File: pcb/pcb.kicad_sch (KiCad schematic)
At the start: 18 parts

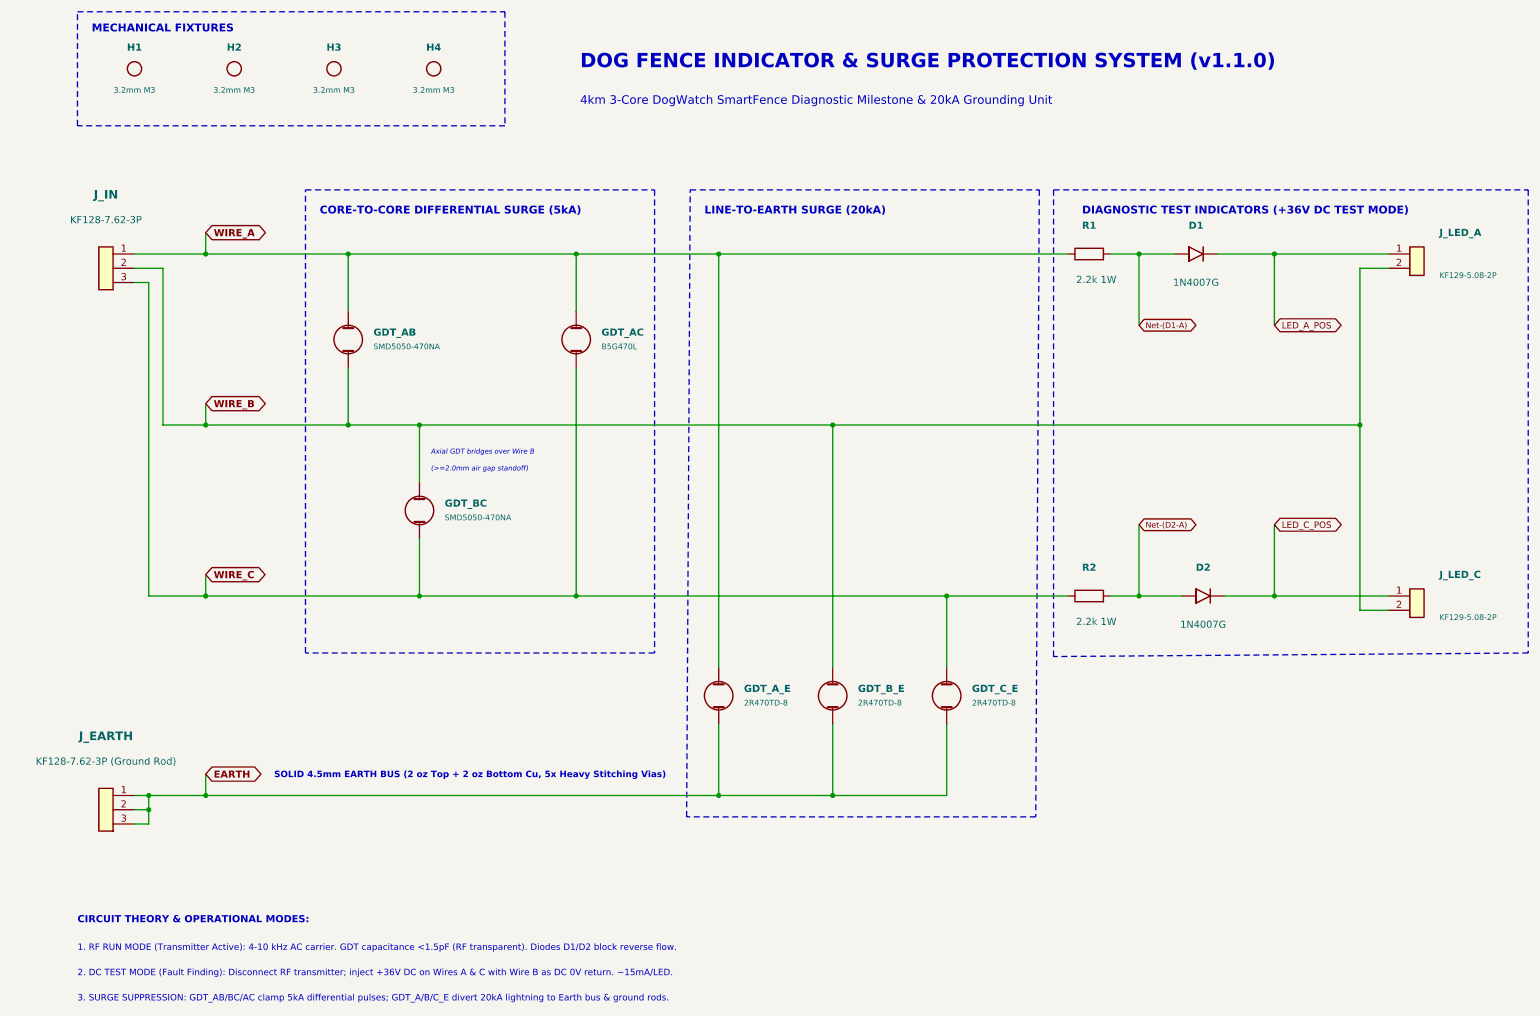
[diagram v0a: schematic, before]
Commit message: Implement guarded remediation and manufacturing verification
Add complete-project checks, native manufacturing validation, electrical regressions, and bounded PCB/library corrections for 1.2.0-dev. Preserve unresolved protection, fit/process, and hardware qualification holds.
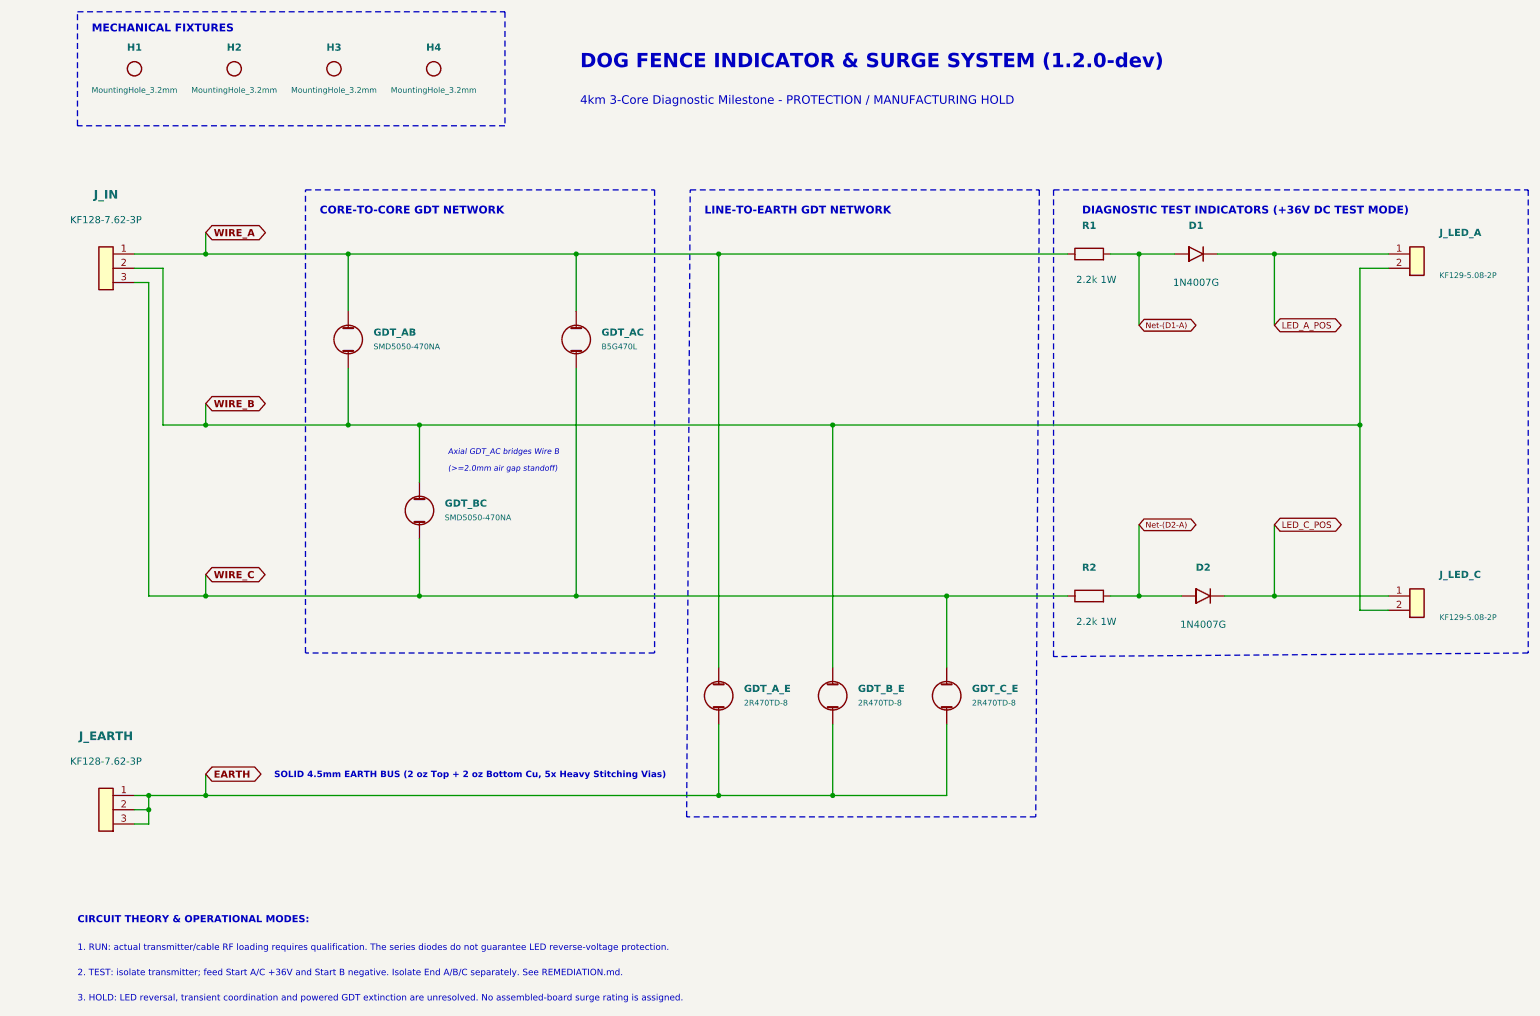
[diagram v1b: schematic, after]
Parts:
- D1, D2: footprint Diode_THT:D_DO-41_SOD81_P10.16mm_Horizontal -> DogFence:1N4007G_P10.16mm_K_Right; symbol Device:D -> DogFence:D_A_Left_K_Right; Manufacturer (none) -> onsemi
- GDT_AB, GDT_BC: footprint GDT_SMD:GDT_SMD_5.0x5.0mm -> DogFence:SMD5050-470NA; symbol Device:GDT -> DogFence:GDT; Manufacturer (none) -> Ruilon
- GDT_AC: footprint Resistor_THT:R_Axial_DIN0617_L17.0mm_D6.0mm_P15.24mm_Horizontal -> DogFence:B5G470L_P15.24mm_NS_Overpass; symbol Device:GDT -> DogFence:GDT; Manufacturer (none) -> Bencent
- GDT_A_E, GDT_B_E, GDT_C_E: footprint Resistor_THT:R_Axial_DIN0617_L17.0mm_D6.0mm_P15.24mm_Horizontal -> DogFence:2R470TD-8_P15.24mm; symbol Device:GDT -> DogFence:GDT; Manufacturer (none) -> Ruilon
- H1, H2, H3, H4: value 3.2mm M3 -> MountingHole_3.2mm; footprint MountingHole:MountingHole_3.2mm_M3 -> DogFence:MountingHole_3.2mm; symbol Mechanical:MountingHole -> DogFence:MountingHole; now left out of the parts list
- J_EARTH: value KF128-7.62-3P (Ground Rod) -> KF128-7.62-3P; footprint TerminalBlock_Phoenix:TerminalBlock_Phoenix_MKDS-1,5-3-7.62_1x03_P7.62mm_Horizontal -> DogFence:KF128_7.62_3P_Earth; symbol Connector_Generic:Conn_01x03 -> DogFence:Conn_01x03; Manufacturer (none) -> Cixi Kefa Elec
- J_IN: footprint TerminalBlock_Phoenix:TerminalBlock_Phoenix_MKDS-1,5-3-7.62_1x03_P7.62mm_Horizontal -> DogFence:KF128_7.62_3P_Input; symbol Connector_Generic:Conn_01x03 -> DogFence:Conn_01x03; Manufacturer (none) -> Cixi Kefa Elec
- J_LED_A: footprint TerminalBlock_Phoenix:TerminalBlock_Phoenix_MKDS-1,5-2-5.08_1x02_P5.08mm_Horizontal -> DogFence:KF129_5.08_2P_LED_A; symbol Connector_Generic:Conn_01x02 -> DogFence:Conn_01x02; Manufacturer (none) -> Cixi Kefa Elec
- J_LED_C: footprint TerminalBlock_Phoenix:TerminalBlock_Phoenix_MKDS-1,5-2-5.08_1x02_P5.08mm_Horizontal -> DogFence:KF129_5.08_2P_LED_C; symbol Connector_Generic:Conn_01x02 -> DogFence:Conn_01x02; Manufacturer (none) -> Cixi Kefa Elec
- R1, R2: footprint Resistor_THT:R_Axial_DIN0414_L11.9mm_D4.5mm_P15.24mm_Horizontal -> DogFence:MBE0414_P15.24mm; symbol Device:R -> DogFence:R; Manufacturer (none) -> Vishay Intertech
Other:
- note added: "1. RUN: actual transmitter/cable RF loading requires qualification. The series diodes do not guarantee LED reverse-voltage protection."
- note added: "2. TEST: isolate transmitter; feed Start A/C +36V and Start B negative. Isolate End A/B/C separately. See REMEDIATION.md."
- note added: "3. HOLD: LED reversal, transient coordination and powered GDT extinction are unresolved. No assembled-board surge rating is assigned."
- note added: "4km 3-Core Diagnostic Milestone - PROTECTION / MANUFACTURING HOLD"
- note added: "Axial GDT_AC bridges Wire B"
- note added: "CORE-TO-CORE GDT NETWORK"
- note added: "DOG FENCE INDICATOR & SURGE SYSTEM (1.2.0-dev)"
- note added: "LINE-TO-EARTH GDT NETWORK"
- note removed: "1. RF RUN MODE (Transmitter Active): 4-10 kHz AC carrier. GDT capacitance <1.5pF (RF transparent). Diodes D1/D2 block reverse flow."
- note removed: "2. DC TEST MODE (Fault Finding): Disconnect RF transmitter; inject +36V DC on Wires A & C with Wire B as DC 0V return. ~15mA/LED."
- note removed: "3. SURGE SUPPRESSION: GDT_AB/BC/AC clamp 5kA differential pulses; GDT_A/B/C_E divert 20kA lightning to Earth bus & ground rods."
- note removed: "4km 3-Core DogWatch SmartFence Diagnostic Milestone & 20kA Grounding Unit"
- note removed: "Axial GDT bridges over Wire B"
- note removed: "CORE-TO-CORE DIFFERENTIAL SURGE (5kA)"
- note removed: "DOG FENCE INDICATOR & SURGE PROTECTION SYSTEM (v1.1.0)"
- note removed: "LINE-TO-EARTH SURGE (20kA)"

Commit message: Add diode to PCB to prevent reverse flow across LEDs
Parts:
- added D3, D4: BYG23T-M3, DogFence:BYG23T_SMA_K_Right, symbol DogFence:D_A_Left_K_Right
- D1, D2: value 1N4007G -> BYG23T-M3; footprint DogFence:1N4007G_P10.16mm_K_Right -> DogFence:BYG23T_SMA_K_Right; LCSC C232439 -> C145454; MPN 1N4007G -> BYG23T-M3/TR; Manufacturer onsemi -> Vishay General Semiconductor; Sourcing (none) -> LCSC
- GDT_AB, GDT_AC, GDT_A_E, GDT_BC, GDT_B_E, GDT_C_E, J_EARTH, J_IN, J_LED_A, J_LED_C: Sourcing (none) -> LCSC
- R1, R2: value 2.2k 1W -> 2.2k 2W; footprint DogFence:MBE0414_P15.24mm -> DogFence:PR02_Cu_P15.24mm; LCSC C1368610 -> (none); MPN MBE04140C2201FC100 -> PR02000202201FA100; Manufacturer Vishay Intertech -> Vishay BCcomponents; Sourcing (none) -> External; Sourcing Reference (none) -> https://www.vishay.com/search?type=inv&query=PR02000202201F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
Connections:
- net LED_A_POS: now also D3.1 (K)
- net LED_C_POS: now also D4.1 (K)
- net WIRE_B: now also D3.2 (A), D4.2 (A)
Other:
- note added: "1. RUN: RF/transient qualification held. D3/D4 clamp negative LED outputs; no reversed flying-lead immunity."
- note added: "2. TEST: isolate transmitter; Start A/C +36V, Start B negative; End A/B/C separately isolated. Continuous-safe duty required; containment disabled."
- note added: "3. HOLD: thermal and powered-GDT recovery unqualified; no board surge rating. Energized cattle fencing prohibited along the entire boundary."
- note removed: "1. RUN: actual transmitter/cable RF loading requires qualification. The series diodes do not guarantee LED reverse-voltage protection."
- note removed: "2. TEST: isolate transmitter; feed Start A/C +36V and Start B negative. Isolate End A/B/C separately. See REMEDIATION.md."
- note removed: "3. HOLD: LED reversal, transient coordination and powered GDT extinction are unresolved. No assembled-board surge rating is assigned."

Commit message: Split prototype/gerbers and release/production makefile output and gates
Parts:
- R1, R2: footprint DogFence:PR02_Cu_P15.24mm -> DogFence:R_2512_6332Metric; LCSC (none) -> C2791283; MPN PR02000202201FA100 -> HP122WF2201T4E; Manufacturer Vishay BCcomponents -> Uni-Royal; Sourcing External -> LCSC; Sourcing Reference https://www.vishay.com/search?type=inv&query=PR02000202201F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 -> (none)
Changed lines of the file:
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@@
 			)
 		)
-		(property "Manufacturer" "Vishay BCcomponents"
+		(property "Manufacturer" "Uni-Royal"
 			(at 205.74 62.23 0)
 			(effects
@@
 			)
 		)
-		(property "Footprint" "DogFence:PR02_Cu_P15.24mm"
+		(property "Footprint" "DogFence:R_2512_6332Metric"
 			(at 205.74 62.23 90)
 			(effects
@@
 			)
 		)
-		(property "Datasheet" "https://www.vishay.com/docs/28729/pr010203.pdf"
+		(property "Datasheet" "https://www.lcsc.com"
 			(at 205.74 62.23 0)
 			(effects
@@
 			)
 		)
-		(property "Description" "Vishay PR02000202201FA100; 2.2k 2W 1%, +/-250ppm/K; Cu lead 0.78 +/-0.05mm, body L2 <=12.0mm D <=3.9mm; require >=1.00mm body-to-PCB standoff; forming/process and continuous TEST thermal qualification held"
+		(property "Description" "Uni-Royal HP122WF2201T4E; 2.2k 2W 1% 2512 SMD chip resistor"
 			(at 205.74 62.23 0)
 			(effects
@@
 			)
 		)
-		(property "MPN" "PR02000202201FA100"
+		(property "MPN" "HP122WF2201T4E"
 			(at 205.74 62.23 0)
 			(effects
@@
 			)
 		)
-		(property "LCSC" ""
+		(property "LCSC" "C2791283"
 			(at 205.74 62.23 0)
 			(effects
@@
 			)
 		)
-		(property "Sourcing" "External"
+		(property "Sourcing" "LCSC"
 			(at 205.74 62.23 0)
 			(effects
@@
 			)
 		)
-		(property "Sourcing Reference" "https://www.vishay.com/search?type=inv&query=PR02000202201FA100"
+		(property "Sourcing Reference" ""
 			(at 205.74 62.23 0)
 			(effects
@@
 			)
 		)
-		(property "Manufacturer" "Vishay BCcomponents"
+		(property "Manufacturer" "Uni-Royal"
 			(at 205.74 123.19 0)
 			(effects
@@
 			)
 		)
-		(property "Footprint" "DogFence:PR02_Cu_P15.24mm"
+		(property "Footprint" "DogFence:R_2512_6332Metric"
 			(at 205.74 123.19 90)
 			(effects
@@
 			)
 		)
-		(property "Datasheet" "https://www.vishay.com/docs/28729/pr010203.pdf"
+		(property "Datasheet" "https://www.lcsc.com"
 			(at 205.74 123.19 0)
 			(effects
@@
 			)
 		)
-		(property "Description" "Vishay PR02000202201FA100; 2.2k 2W 1%, +/-250ppm/K; Cu lead 0.78 +/-0.05mm, body L2 <=12.0mm D <=3.9mm; require >=1.00mm body-to-PCB standoff; forming/process and continuous TEST thermal qualification held"
+		(property "Description" "Uni-Royal HP122WF2201T4E; 2.2k 2W 1% 2512 SMD chip resistor"
 			(at 205.74 123.19 0)
 			(effects
@@
 			)
 		)
-		(property "MPN" "PR02000202201FA100"
+		(property "MPN" "HP122WF2201T4E"
 			(at 205.74 123.19 0)
 			(effects
@@
 			)
 		)
-		(property "LCSC" ""
+		(property "LCSC" "C2791283"
 			(at 205.74 123.19 0)
 			(effects
@@
 			)
 		)
-		(property "Sourcing" "External"
+		(property "Sourcing" "LCSC"
 			(at 205.74 123.19 0)
 			(effects
@@
 			)
 		)
-		(property "Sourcing Reference" "https://www.vishay.com/search?type=inv&query=PR02000202201FA100"
+		(property "Sourcing Reference" ""
 			(at 205.74 123.19 0)
 			(effects

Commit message: Review of Gemini simplification by GPT
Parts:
- R1, R2: LCSC C2791283 -> (none); Sourcing LCSC -> External; Sourcing Reference (none) -> https://store.nacsemi.com/products/detail?stock=XSJMZ000001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
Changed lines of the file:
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@@
 			)
 		)
-		(property "Datasheet" "https://www.lcsc.com"
+		(property "Datasheet" "https://www.uni-royal.cn/en/images/userfile/file/1784806233a2e6d381ea80b5d9.pdf"
 			(at 205.74 62.23 0)
 			(effects
@@
 			)
 		)
-		(property "LCSC" "C2791283"
+		(property "LCSC" ""
 			(at 205.74 62.23 0)
 			(effects
@@
 			)
 		)
-		(property "Sourcing" "LCSC"
+		(property "Sourcing" "External"
 			(at 205.74 62.23 0)
 			(effects
@@
 			)
 		)
-		(property "Sourcing Reference" ""
+		(property "Sourcing Reference" "https://store.nacsemi.com/products/detail?stock=XSJMZ0000010410"
 			(at 205.74 62.23 0)
 			(effects
@@
 			)
 		)
-		(property "Datasheet" "https://www.lcsc.com"
+		(property "Datasheet" "https://www.uni-royal.cn/en/images/userfile/file/1784806233a2e6d381ea80b5d9.pdf"
 			(at 205.74 123.19 0)
 			(effects
@@
 			)
 		)
-		(property "LCSC" "C2791283"
+		(property "LCSC" ""
 			(at 205.74 123.19 0)
 			(effects
@@
 			)
 		)
-		(property "Sourcing" "LCSC"
+		(property "Sourcing" "External"
 			(at 205.74 123.19 0)
 			(effects
@@
 			)
 		)
-		(property "Sourcing Reference" ""
+		(property "Sourcing Reference" "https://store.nacsemi.com/products/detail?stock=XSJMZ0000010410"
 			(at 205.74 123.19 0)
 			(effects

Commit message: Finalize R1/R2 as Uni-Royal PS122WF2201T4E
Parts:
- R1, R2: LCSC (none) -> C2793873; MPN HP122WF2201T4E -> PS122WF2201T4E; Sourcing External -> LCSC; Sourcing Reference https://store.nacsemi.com/products/detail?stock=XSJMZ000001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 -> (none)
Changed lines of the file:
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@@
 			)
 		)
-		(property "Datasheet" "https://www.uni-royal.cn/en/images/userfile/file/1784806233a2e6d381ea80b5d9.pdf"
+		(property "Datasheet" "https://www.uni-royal.cn/en/images/userfile/file/1784854235b7c79f8d8a205c5d.pdf"
 			(at 205.74 62.23 0)
 			(effects
@@
 			)
 		)
-		(property "Description" "Uni-Royal HP122WF2201T4E; 2.2k 2W 1% 2512 SMD chip resistor"
+		(property "Description" "Uni-Royal PS122WF2201T4E C2793873; 2.2k 2W 1% PS12/2512 SMD chip resistor; prototype and production"
 			(at 205.74 62.23 0)
 			(effects
@@
 			)
 		)
-		(property "MPN" "HP122WF2201T4E"
+		(property "MPN" "PS122WF2201T4E"
 			(at 205.74 62.23 0)
 			(effects
@@
 			)
 		)
-		(property "LCSC" ""
+		(property "LCSC" "C2793873"
 			(at 205.74 62.23 0)
 			(effects
@@
 			)
 		)
-		(property "Sourcing" "External"
+		(property "Sourcing" "LCSC"
 			(at 205.74 62.23 0)
 			(effects
@@
 			)
 		)
-		(property "Sourcing Reference" "https://store.nacsemi.com/products/detail?stock=XSJMZ0000010410"
+		(property "Sourcing Reference" ""
 			(at 205.74 62.23 0)
 			(effects
@@
 			)
 		)
-		(property "Datasheet" "https://www.uni-royal.cn/en/images/userfile/file/1784806233a2e6d381ea80b5d9.pdf"
+		(property "Datasheet" "https://www.uni-royal.cn/en/images/userfile/file/1784854235b7c79f8d8a205c5d.pdf"
 			(at 205.74 123.19 0)
 			(effects
@@
 			)
 		)
-		(property "Description" "Uni-Royal HP122WF2201T4E; 2.2k 2W 1% 2512 SMD chip resistor"
+		(property "Description" "Uni-Royal PS122WF2201T4E C2793873; 2.2k 2W 1% PS12/2512 SMD chip resistor; prototype and production"
 			(at 205.74 123.19 0)
 			(effects
@@
 			)
 		)
-		(property "MPN" "HP122WF2201T4E"
+		(property "MPN" "PS122WF2201T4E"
 			(at 205.74 123.19 0)
 			(effects
@@
 			)
 		)
-		(property "LCSC" ""
+		(property "LCSC" "C2793873"
 			(at 205.74 123.19 0)
 			(effects
@@
 			)
 		)
-		(property "Sourcing" "External"
+		(property "Sourcing" "LCSC"
 			(at 205.74 123.19 0)
 			(effects
@@
 			)
 		)
-		(property "Sourcing Reference" "https://store.nacsemi.com/products/detail?stock=XSJMZ0000010410"
+		(property "Sourcing Reference" ""
 			(at 205.74 123.19 0)
 			(effects

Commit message: Move to a TE R1/R2 prototype with Yageo for production
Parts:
- R1, R2: LCSC C2793873 -> C4129105; MPN PS122WF2201T4E -> 35212K2FT; Manufacturer Uni-Royal -> TE Connectivity
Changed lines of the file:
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@@
 			)
 		)
-		(property "Manufacturer" "Uni-Royal"
+		(property "Manufacturer" "TE Connectivity"
 			(at 205.74 62.23 0)
 			(effects
@@
 			)
 		)
-		(property "Datasheet" "https://www.uni-royal.cn/en/images/userfile/file/1784854235b7c79f8d8a205c5d.pdf"
+		(property "Datasheet" "https://www.te.com/commerce/DocumentDelivery/DDEController?Action=showdoc&DocId=Data+Sheet%7F9-1773463-5%7FG1%7Fpdf%7FEnglish%7FENG_DS_9-1773463-5_G1.pdf"
 			(at 205.74 62.23 0)
 			(effects
@@
 			)
 		)
-		(property "Description" "Uni-Royal PS122WF2201T4E C2793873; 2.2k 2W 1% PS12/2512 SMD chip resistor; prototype and production"
+		(property "Description" "TE Connectivity 35212K2FT C4129105; 2.2k 2W 1% 3521/2512 SMD chip resistor; prototype selection"
 			(at 205.74 62.23 0)
 			(effects
@@
 			)
 		)
-		(property "MPN" "PS122WF2201T4E"
+		(property "MPN" "35212K2FT"
 			(at 205.74 62.23 0)
 			(effects
@@
 			)
 		)
-		(property "LCSC" "C2793873"
+		(property "LCSC" "C4129105"
 			(at 205.74 62.23 0)
 			(effects
@@
 			)
 		)
-		(property "Manufacturer" "Uni-Royal"
+		(property "Manufacturer" "TE Connectivity"
 			(at 205.74 123.19 0)
 			(effects
@@
 			)
 		)
-		(property "Datasheet" "https://www.uni-royal.cn/en/images/userfile/file/1784854235b7c79f8d8a205c5d.pdf"
+		(property "Datasheet" "https://www.te.com/commerce/DocumentDelivery/DDEController?Action=showdoc&DocId=Data+Sheet%7F9-1773463-5%7FG1%7Fpdf%7FEnglish%7FENG_DS_9-1773463-5_G1.pdf"
 			(at 205.74 123.19 0)
 			(effects
@@
 			)
 		)
-		(property "Description" "Uni-Royal PS122WF2201T4E C2793873; 2.2k 2W 1% PS12/2512 SMD chip resistor; prototype and production"
+		(property "Description" "TE Connectivity 35212K2FT C4129105; 2.2k 2W 1% 3521/2512 SMD chip resistor; prototype selection"
 			(at 205.74 123.19 0)
 			(effects
@@
 			)
 		)
-		(property "MPN" "PS122WF2201T4E"
+		(property "MPN" "35212K2FT"
 			(at 205.74 123.19 0)
 			(effects
@@
 			)
 		)
-		(property "LCSC" "C2793873"
+		(property "LCSC" "C4129105"
 			(at 205.74 123.19 0)
 			(effects
